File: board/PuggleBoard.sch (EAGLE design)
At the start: 127 parts, among them U1 OPA4209, U10 24C, U2 ADS8331, U3 AD5686, U4 OPA4209, U5 LM2663, U6 TPS7A3001, U7 TPS7A4901, U8 REF5040, U9 AD8032

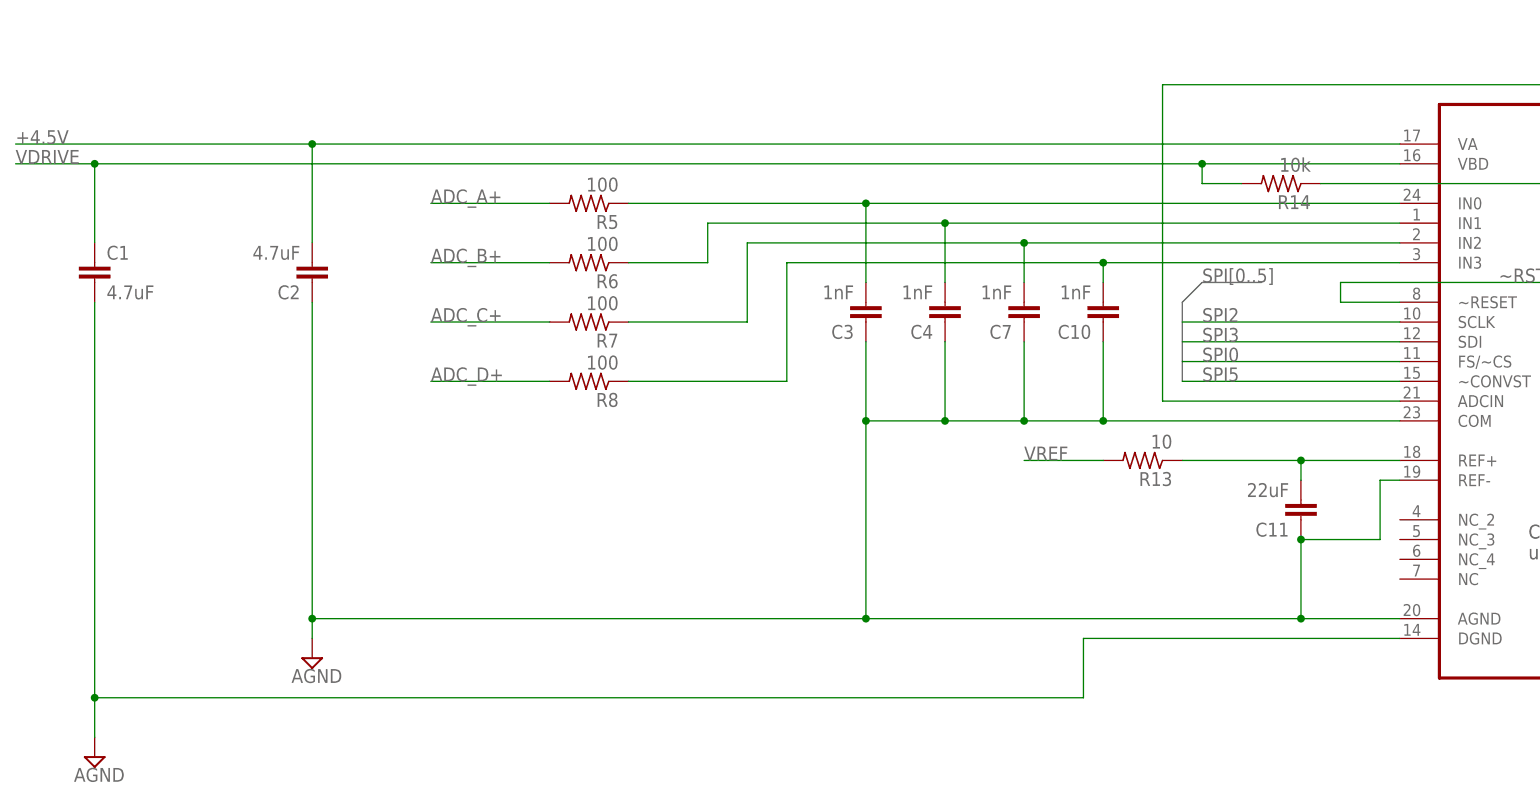
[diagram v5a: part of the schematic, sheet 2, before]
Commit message: Layout of ADC power bypassing and input filtering.
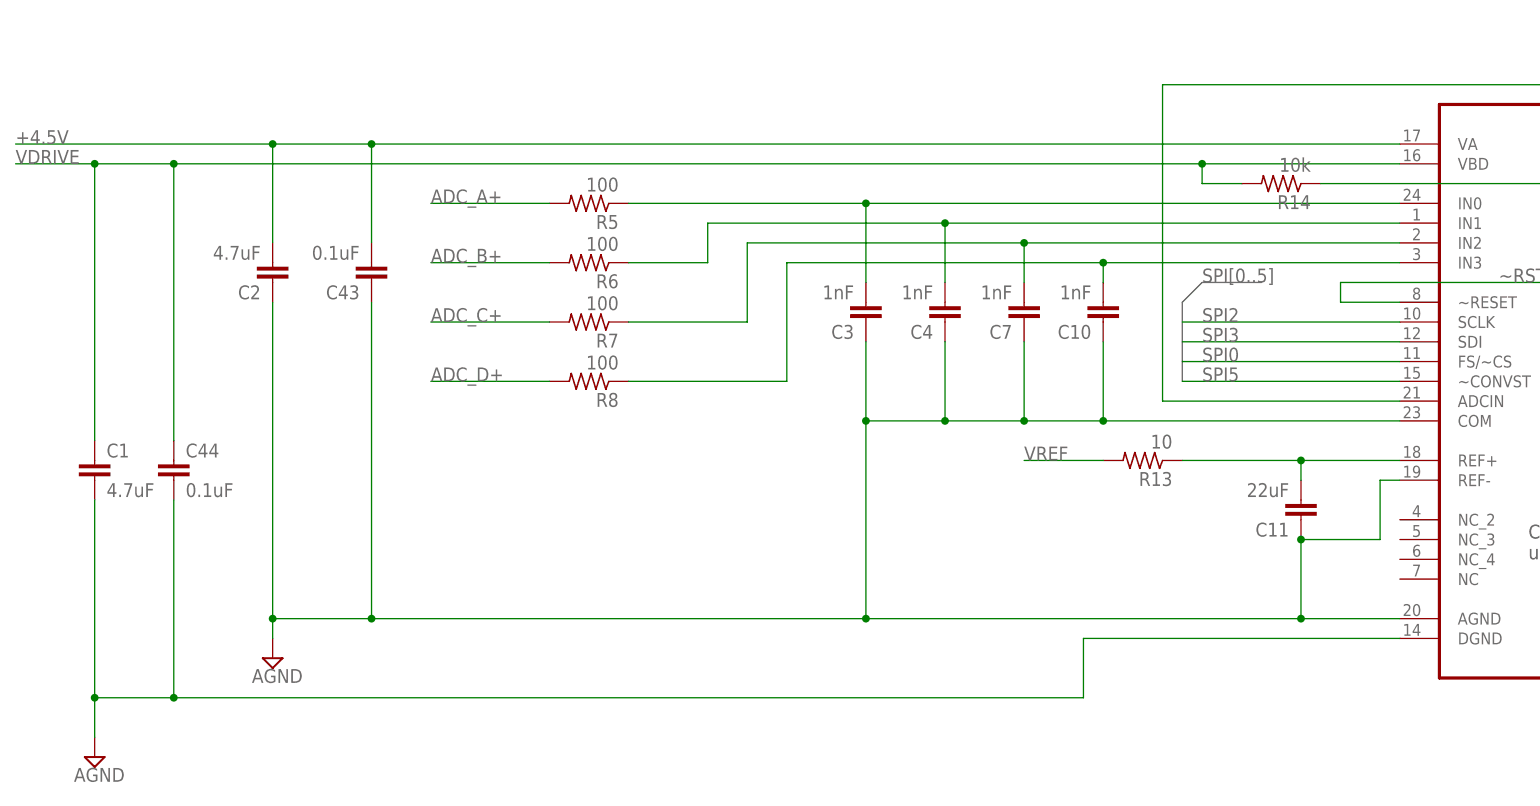
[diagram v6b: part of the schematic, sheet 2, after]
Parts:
- added C43, C44: 0.1uF, rcl:C-EUC0603
- C11: device rcl:C-EUC0603 -> rcl:C-EUC0805
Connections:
- removed net ADC_SPI1: BB1.GPIO2_23
- removed net ADC_SPI2: BB1.GPIO2_22
- removed net DAC_SPI0: BB1.GPIO1_31
- removed net DAC_SPI1: BB1.GPIO2_24
- removed net DAC_SPI2: BB1.GPIO1_30
- removed net SPI_CLK: BB1.GPIO2_25
- net +4.5V: now also C43.2
- net AGND: now also C43.1, C44.2
- net SPI0: now also BB1.GPIO1_31
- net SPI1: now also BB1.GPIO2_23, BB1.GPIO2_24
- net SPI2: now also BB1.GPIO1_30, BB1.GPIO2_22
- net SPI5: now also BB1.GPIO2_25
- net VDRIVE: now also C44.1
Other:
- moved on the sheet: C1, C2
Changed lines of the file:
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@@
 <part name="VREF_PRE" library="testpad" deviceset="TP" device="B1,27"/>
 <part name="C2" library="rcl" deviceset="C-EU" device="C0805" value="4.7uF"/>
-<part name="C11" library="rcl" deviceset="C-EU" device="C0603" value="22uF"/>
+<part name="C11" library="rcl" deviceset="C-EU" device="C0805" value="22uF"/>
 <part name="C1" library="rcl" deviceset="C-EU" device="C0805" value="4.7uF"/>
 <part name="SUPPLY11" library="supply2" deviceset="AGND" device=""/>
@@
 <part name="C27" library="rcl" deviceset="C-EU" device="C0603" value="10nF"/>
 <part name="SUPPLY27" library="supply2" deviceset="AGND" device=""/>
+<part name="C43" library="rcl" deviceset="C-EU" device="C0603" value="0.1uF"/>
+<part name="C44" library="rcl" deviceset="C-EU" device="C0603" value="0.1uF"/>
 </parts>
 <sheets>
@@
 </segment>
 </net>
-<net name="ADC_SPI1" class="0">
-<segment>
-<pinref part="BB1" gate="G$1" pin="GPIO2_23"/>
-<wire x1="-63.5" y1="73.66" x2="-81.28" y2="73.66" width="0.1524" layer="91"/>
-<label x="-81.28" y="73.66" size="1.778" layer="95"/>
-</segment>
-</net>
-<net name="ADC_SPI2" class="0">
-<segment>
-<pinref part="BB1" gate="G$1" pin="GPIO2_22"/>
-<wire x1="-63.5" y1="76.2" x2="-81.28" y2="76.2" width="0.1524" layer="91"/>
-<label x="-81.28" y="76.2" size="1.778" layer="95"/>
-</segment>
-</net>
-<net name="SPI_CLK" class="0">
-<segment>
-<pinref part="BB1" gate="G$1" pin="GPIO2_25"/>
-<wire x1="-7.62" y1="73.66" x2="10.16" y2="73.66" width="0.1524" layer="91"/>
-<label x="-2.54" y="73.66" size="1.778" layer="95"/>
-</segment>
-</net>
-<net name="DAC_SPI1" class="0">
-<segment>
-<pinref part="BB1" gate="G$1" pin="GPIO2_24"/>
-<wire x1="-7.62" y1="76.2" x2="10.16" y2="76.2" width="0.1524" layer="91"/>
-<label x="-2.54" y="76.2" size="1.778" layer="95"/>
-</segment>
-</net>
-<net name="DAC_SPI2" class="0">
-<segment>
-<pinref part="BB1" gate="G$1" pin="GPIO1_30"/>
-<wire x1="-63.5" y1="83.82" x2="-81.28" y2="83.82" width="0.1524" layer="91"/>
-<label x="-81.28" y="83.82" size="1.778" layer="95"/>
-</segment>
-</net>
 <net name="~RST" class="0">
 <segment>
@@
 </segment>
 </net>
-<net name="DAC_SPI0" class="0">
+<net name="SPI0" class="0">
+<segment>
+<wire x1="55.88" y1="81.28" x2="43.18" y2="81.28" width="0.1524" layer="91"/>
+<label x="43.18" y="81.28" size="1.778" layer="95"/>
+</segment>
 <segment>
 <pinref part="BB1" gate="G$1" pin="GPIO1_31"/>
@@
 </segment>
 </net>
-<net name="SPI0" class="0">
-<segment>
-<wire x1="55.88" y1="81.28" x2="43.18" y2="81.28" width="0.1524" layer="91"/>
-<label x="43.18" y="81.28" size="1.778" layer="95"/>
-</segment>
-</net>
 <net name="SPI1" class="0">
 <segment>
@@
 <label x="43.18" y="78.74" size="1.778" layer="95"/>
 </segment>
+<segment>
+<pinref part="BB1" gate="G$1" pin="GPIO2_23"/>
+<wire x1="-63.5" y1="73.66" x2="-81.28" y2="73.66" width="0.1524" layer="91"/>
+<label x="-81.28" y="73.66" size="1.778" layer="95"/>
+</segment>
+<segment>
+<pinref part="BB1" gate="G$1" pin="GPIO2_24"/>
+<wire x1="-7.62" y1="76.2" x2="10.16" y2="76.2" width="0.1524" layer="91"/>
+<label x="-2.54" y="76.2" size="1.778" layer="95"/>
+</segment>
 </net>
 <net name="SPI2" class="0">
@@
 <label x="43.18" y="76.2" size="1.778" layer="95"/>
 </segment>
+<segment>
+<pinref part="BB1" gate="G$1" pin="GPIO1_30"/>
+<wire x1="-63.5" y1="83.82" x2="-81.28" y2="83.82" width="0.1524" layer="91"/>
+<label x="-81.28" y="83.82" size="1.778" layer="95"/>
+</segment>
+<segment>
+<pinref part="BB1" gate="G$1" pin="GPIO2_22"/>
+<wire x1="-63.5" y1="76.2" x2="-81.28" y2="76.2" width="0.1524" layer="91"/>
+<label x="-81.28" y="76.2" size="1.778" layer="95"/>
+</segment>
 </net>
 <net name="SPI3" class="0">
@@
 <wire x1="55.88" y1="68.58" x2="43.18" y2="68.58" width="0.1524" layer="91"/>
 <label x="43.18" y="68.58" size="1.778" layer="95"/>
+</segment>
+<segment>
+<pinref part="BB1" gate="G$1" pin="GPIO2_25"/>
+<wire x1="-7.62" y1="73.66" x2="10.16" y2="73.66" width="0.1524" layer="91"/>
+<label x="-2.54" y="73.66" size="1.778" layer="95"/>
 </segment>
 </net>
@@
 <instance part="R2" gate="G$1" x="-104.14" y="187.96" rot="R180"/>
 <instance part="R4" gate="G$1" x="-93.98" y="177.8" rot="R90"/>
-<instance part="C2" gate="G$1" x="-88.9" y="78.74" rot="R180"/>
+<instance part="C2" gate="G$1" x="-93.98" y="78.74" rot="R180"/>
 <instance part="C11" gate="G$1" x="38.1" y="48.26" rot="R180"/>
-<instance part="C1" gate="G$1" x="-116.84" y="81.28"/>
-<instance part="SUPPLY11" gate="G$1" x="-88.9" y="30.48"/>
+<instance part="C1" gate="G$1" x="-116.84" y="55.88"/>
+<instance part="SUPPLY11" gate="G$1" x="-93.98" y="30.48"/>
 <instance part="C9" gate="G$1" x="12.7" y="147.32"/>
 <instance part="C8" gate="G$1" x="12.7" y="175.26"/>
@@
 <instance part="R12" gate="G$1" x="-38.1" y="139.7" rot="R90"/>
 <instance part="SUPPLY9" gate="G$1" x="-116.84" y="17.78"/>
+<instance part="C43" gate="G$1" x="-81.28" y="78.74" rot="R180"/>
+<instance part="C44" gate="G$1" x="-106.68" y="55.88"/>
 </instances>
 <busses>
@@
 <segment>
 <pinref part="U2" gate="A" pin="VA"/>
-<wire x1="50.8" y1="96.52" x2="-88.9" y2="96.52" width="0.1524" layer="91"/>
+<wire x1="50.8" y1="96.52" x2="-81.28" y2="96.52" width="0.1524" layer="91"/>
 <pinref part="C2" gate="G$1" pin="2"/>
-<wire x1="-88.9" y1="96.52" x2="-127" y2="96.52" width="0.1524" layer="91"/>
-<wire x1="-88.9" y1="83.82" x2="-88.9" y2="96.52" width="0.1524" layer="91"/>
-<junction x="-88.9" y="96.52"/>
+<wire x1="-81.28" y1="96.52" x2="-93.98" y2="96.52" width="0.1524" layer="91"/>
+<wire x1="-93.98" y1="96.52" x2="-127" y2="96.52" width="0.1524" layer="91"/>
+<wire x1="-93.98" y1="83.82" x2="-93.98" y2="96.52" width="0.1524" layer="91"/>
+<junction x="-93.98" y="96.52"/>
 <label x="-127" y="96.52" size="1.778" layer="95"/>
+<pinref part="C43" gate="G$1" pin="2"/>
+<wire x1="-81.28" y1="83.82" x2="-81.28" y2="96.52" width="0.1524" layer="91"/>
+<junction x="-81.28" y="96.52"/>
 </segment>
 <segment>
@@
 <segment>
 <pinref part="C1" gate="G$1" pin="1"/>
-<wire x1="-116.84" y1="93.98" x2="-116.84" y2="83.82" width="0.1524" layer="91"/>
+<wire x1="-116.84" y1="93.98" x2="-116.84" y2="58.42" width="0.1524" layer="91"/>
 <junction x="-116.84" y="93.98"/>
 <pinref part="U2" gate="A" pin="VBD"/>
-<wire x1="-116.84" y1="93.98" x2="25.4" y2="93.98" width="0.1524" layer="91"/>
+<wire x1="-116.84" y1="93.98" x2="-106.68" y2="93.98" width="0.1524" layer="91"/>
 <pinref part="R14" gate="G$1" pin="2"/>
+<wire x1="-106.68" y1="93.98" x2="25.4" y2="93.98" width="0.1524" layer="91"/>
 <wire x1="25.4" y1="93.98" x2="50.8" y2="93.98" width="0.1524" layer="91"/>
 <wire x1="30.48" y1="91.44" x2="25.4" y2="91.44" width="0.1524" layer="91"/>
@@
 <wire x1="-116.84" y1="93.98" x2="-127" y2="93.98" width="0.1524" layer="91"/>
 <label x="-127" y="93.98" size="1.778" layer="95"/>
+<pinref part="C44" gate="G$1" pin="1"/>
+<wire x1="-106.68" y1="58.42" x2="-106.68" y2="93.98" width="0.1524" layer="91"/>
+<junction x="-106.68" y="93.98"/>
 </segment>
 </net>
@@
 <wire x1="50.8" y1="35.56" x2="38.1" y2="35.56" width="0.1524" layer="91"/>
 <wire x1="38.1" y1="35.56" x2="-17.78" y2="35.56" width="0.1524" layer="91"/>
-<wire x1="-17.78" y1="35.56" x2="-88.9" y2="35.56" width="0.1524" layer="91"/>
-<wire x1="-88.9" y1="35.56" x2="-88.9" y2="76.2" width="0.1524" layer="91"/>
+<wire x1="-17.78" y1="35.56" x2="-81.28" y2="35.56" width="0.1524" layer="91"/>
+<wire x1="-81.28" y1="35.56" x2="-93.98" y2="35.56" width="0.1524" layer="91"/>
+<wire x1="-93.98" y1="35.56" x2="-93.98" y2="76.2" width="0.1524" layer="91"/>
 <pinref part="C2" gate="G$1" pin="1"/>
-<wire x1="-88.9" y1="35.56" x2="-88.9" y2="33.02" width="0.1524" layer="91"/>
-<junction x="-88.9" y="35.56"/>
+<wire x1="-93.98" y1="35.56" x2="-93.98" y2="33.02" width="0.1524" layer="91"/>
+<junction x="-93.98" y="35.56"/>
 <wire x1="38.1" y1="45.72" x2="38.1" y2="35.56" width="0.1524" layer="91"/>
 <junction x="38.1" y="45.72"/>
@@
 <junction x="-17.78" y="60.96"/>
 <junction x="-17.78" y="35.56"/>
+<pinref part="C43" gate="G$1" pin="1"/>
+<wire x1="-81.28" y1="76.2" x2="-81.28" y2="35.56" width="0.1524" layer="91"/>
+<junction x="-81.28" y="35.56"/>
 </segment>
 <segment>
@@
 <segment>
 <pinref part="C1" gate="G$1" pin="2"/>
-<wire x1="-116.84" y1="76.2" x2="-116.84" y2="25.4" width="0.1524" layer="91"/>
+<wire x1="-116.84" y1="50.8" x2="-116.84" y2="25.4" width="0.1524" layer="91"/>
 <pinref part="U2" gate="A" pin="DGND"/>
 <wire x1="50.8" y1="33.02" x2="10.16" y2="33.02" width="0.1524" layer="91"/>
 <wire x1="10.16" y1="33.02" x2="10.16" y2="25.4" width="0.1524" layer="91"/>
-<wire x1="10.16" y1="25.4" x2="-116.84" y2="25.4" width="0.1524" layer="91"/>
+<wire x1="10.16" y1="25.4" x2="-106.68" y2="25.4" width="0.1524" layer="91"/>
 <pinref part="SUPPLY9" gate="G$1" pin="AGND"/>
+<wire x1="-106.68" y1="25.4" x2="-116.84" y2="25.4" width="0.1524" layer="91"/>
 <wire x1="-116.84" y1="20.32" x2="-116.84" y2="25.4" width="0.1524" layer="91"/>
 <junction x="-116.84" y="25.4"/>
-</segment>
-</net>
+<pinref part="C44" gate="G$1" pin="2"/>
+<wire x1="-106.68" y1="50.8" x2="-106.68" y2="25.4" width="0.1524" layer="91"/>
+<junction x="-106.68" y="25.4"/>
+</segment>
+</net>

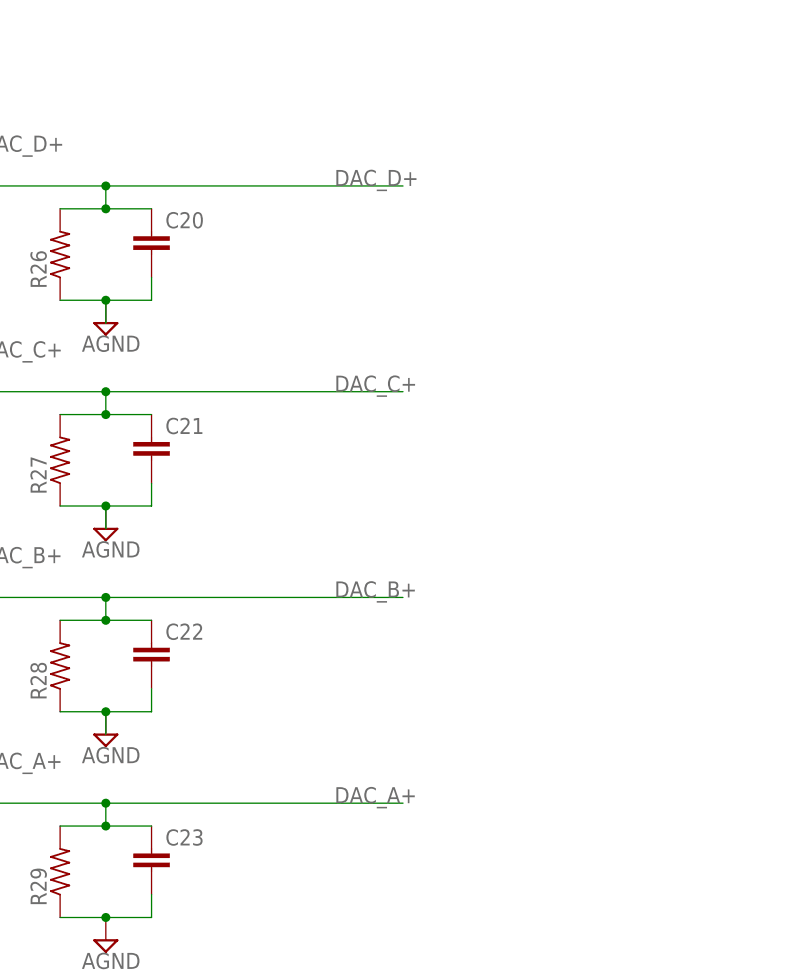
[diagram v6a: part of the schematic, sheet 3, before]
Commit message: Finished op-amp pattern on DAC side. Basically will copy for ADC buffer.
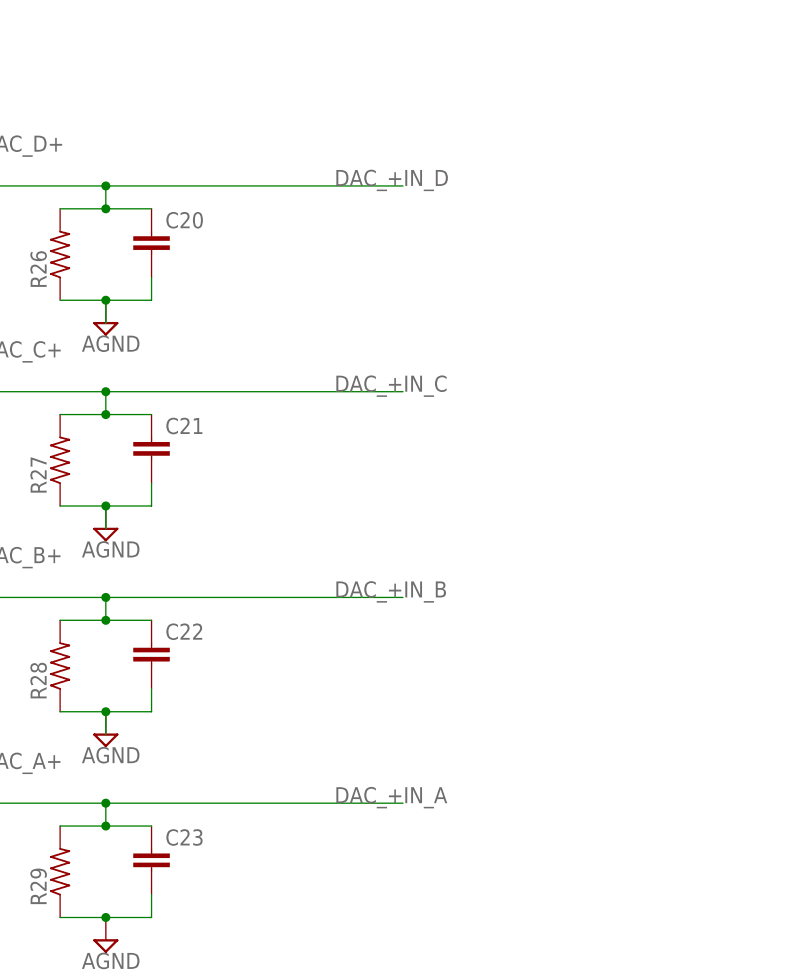
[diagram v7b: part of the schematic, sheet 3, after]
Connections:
- removed net DAC_A+: C23.1, DAC_A+.TP, R29.2, U3.VOUTA
- removed net DAC_B+: C22.1, DAC_B+.TP, R28.2, U3.VOUTB
- removed net DAC_C+: C21.1, DAC_C+.TP, R27.2, U3.VOUTC
- removed net DAC_D+: C20.1, DAC_D+.TP, R26.2, U3.VOUTD
- new net N$6: A_I/O.3
- new net N$8: A_I/O.9
- net DAC_+IN_A: now also C23.1, DAC_A+.TP, R29.2, U3.VOUTA
- net DAC_+IN_B: now also C22.1, DAC_B+.TP, R28.2, U3.VOUTB
- net DAC_+IN_C: now also C21.1, DAC_C+.TP, R27.2, U3.VOUTC
- net DAC_+IN_D: now also C20.1, DAC_D+.TP, R26.2, U3.VOUTD
- net DAC_A: no longer A_I/O.3
- net DAC_D: no longer A_I/O.9
